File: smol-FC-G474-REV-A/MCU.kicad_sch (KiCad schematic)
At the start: 1 part, among them U1 STM32G474RETx

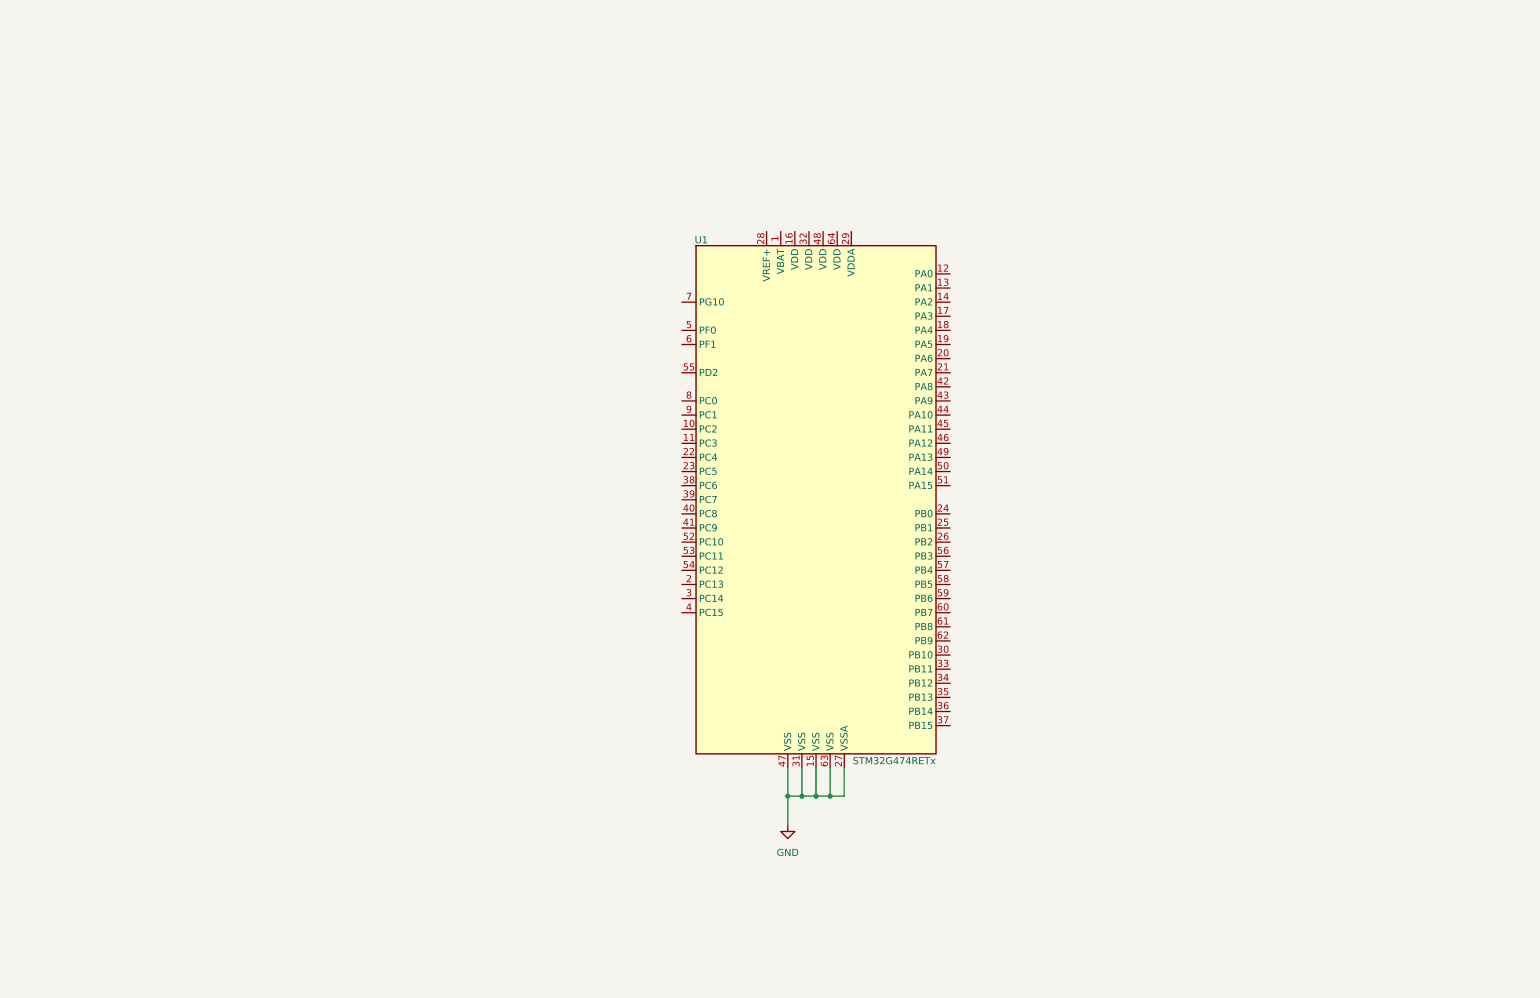
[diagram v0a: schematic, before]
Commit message: added USB-C section
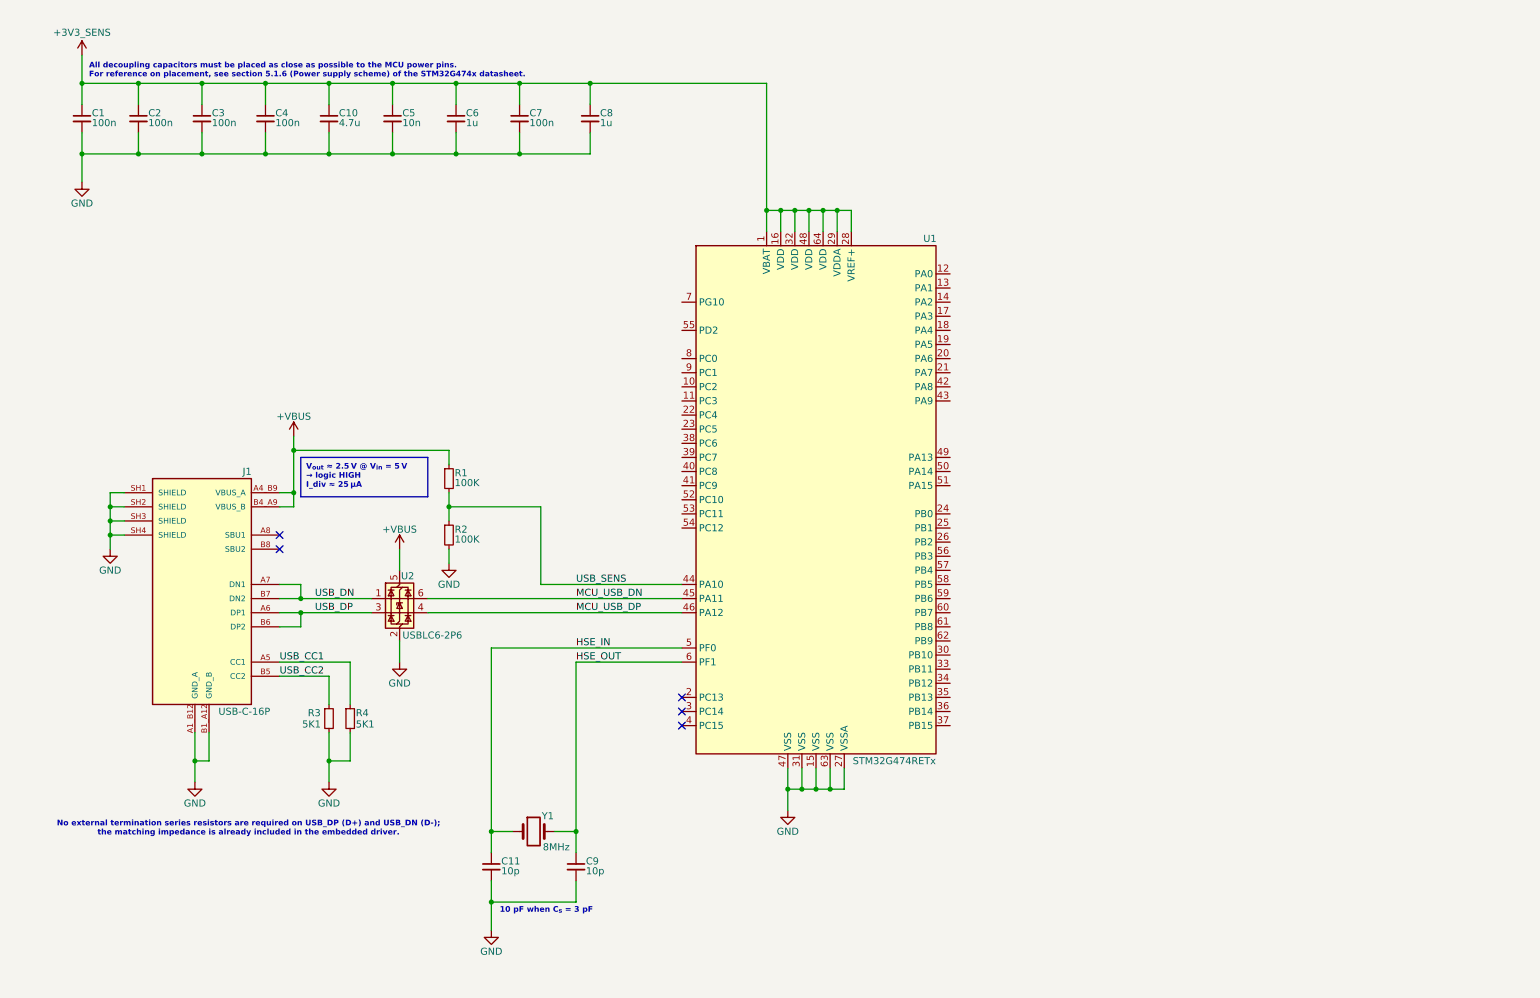
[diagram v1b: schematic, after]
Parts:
- added C1, C2, C3, C4, C7: 100n, symbol Device:C_Small
- added C10: 4.7u, symbol Device:C_Small
- added C11, C9: 10p, symbol Device:C_Small
- added C5: 10n, symbol Device:C_Small
- added C6, C8: 1u, symbol Device:C_Small
- added J1: USB-C-16P, TYPE-C_16PIN_2MD__073_:SHOUHAN_TYPE-C_16PIN_2MD__073_, symbol TYPE-C_16PIN_2MD__073_:TYPE-C_16PIN_2MD__073_
- added R1, R2: 100K, symbol Device:R_Small
- added R3, R4: 5K1, symbol Device:R_Small
- added U2: USBLC6-2P6, Package_TO_SOT_SMD:SOT-666, symbol Power_Protection:USBLC6-2P6
- added Y1: 8MHz, symbol Device:Crystal
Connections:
- net GND: now also C1.2, C10.2, C11.2, C2.2, C3.2, C4.2, C5.2, C6.2, C7.2, C8.2, C9.2, J1.A1_B12 (GND_A), J1.B1_A12 (GND_B), J1.SH1 (SHIELD), J1.SH2 (SHIELD), J1.SH3 (SHIELD), J1.SH4 (SHIELD), R2.2, R3.2, R4.2, U2.2 (GND)
- net +3V3_SENS: now reaches U1.1 (VBAT)
- net +3V3_SENS: now also U1.16 (VDD), U1.28 (VREF+), U1.29 (VDDA), U1.32 (VDD), U1.48 (VDD), U1.64 (VDD), C1.1, C10.1, C2.1, C3.1, C4.1, C5.1, C6.1, C7.1, C8.1
- net USB_SENS: now reaches U1.44 (PA10)
- net USB_SENS: now also R1.2, R2.1
- net MCU_USB_DN: now reaches U1.45 (PA11)
- net MCU_USB_DN: now also U2.6 (I/O1)
- net MCU_USB_DP: now reaches U1.46 (PA12)
- net MCU_USB_DP: now also U2.4 (I/O2)
- net HSE_IN: now reaches U1.5 (PF0)
- net HSE_IN: now also C11.1, Y1.1
- net HSE_OUT: now reaches U1.6 (PF1)
- net HSE_OUT: now also C9.1, Y1.2
- new net +VBUS: J1.A4_B9 (VBUS_A), J1.B4_A9 (VBUS_B), R1.1, U2.5 (VBUS)
- new net USB_CC1: J1.A5 (CC1), R4.1
- new net USB_CC2: J1.B5 (CC2), R3.1
- new net USB_DN: J1.A7 (DN1), J1.B7 (DN2), U2.1 (I/O1)
- new net USB_DP: J1.A6 (DP1), J1.B6 (DP2), U2.3 (I/O2)
- no-connect marks 0 -> 5
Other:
- note added: "10 pF when C_{s} = 3 pF"
- note added: "All decoupling capacitors must be placed as close as possible to the MCU power pins. For reference on placement, see section 5.1.6 (Power supply scheme) of the STM32G474x datasheet."
- note added: "No external termination series resistors are required on USB_DP (D+) and USB_DN (D-); the matching impedance is already included in the embedded driver."

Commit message: Schematic update
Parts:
- added 3V3_CORE, GND, NRST, SWCLK, SWDIO: TestPoint, symbol Connector:TestPoint
- added C10, C11, C14: 100n, symbol Device:C_Small
- added D1, D2, D3: LED, symbol Device:LED
- added D4: ESD, ESDALC6V1-1U2:DIODE_ESDALC6V1-1U2, symbol ESDALC6V1-1U2:ESDALC6V1-1U2
- added D5: RED, symbol Device:LED
- added R1, R12, R2, R3: 1K, symbol Device:R_Small
- added R10, R11, R5: 10K, symbol Device:R_Small
- added R4: 100K, symbol Device:R_Small
- added SW1: BOOT, symbol Switch:SW_Push
- renumbered C11 to C12, C9 to C13, C10 to C5, C5 to C6, C6 to C7, C7 to C8, C8 to C9, R1 to R6, R2 to R7, R3 to R8, R4 to R9
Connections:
- net GND: now also C10.2, C11.2, C14.2, D4.2, D5.1 (K), GND.1, R10.2, R5.2
- net M3: now reaches U1.10 (PC2)
- net M4: now reaches U1.11 (PC3)
- net ADC_CURR: now reaches U1.12 (PA0)
- net ADC_CURR: now also C11.1
- net ADC_VBAT: now reaches U1.13 (PA1)
- net ADC_VBAT: now also C10.1, R4.2, R5.1
- net TX2 (VTX): now reaches U1.14 (PA2)
- net RX2 (VTX): now reaches U1.17 (PA3)
- net SPI1_CS (OSD): now reaches U1.18 (PA4)
- net SPI1_SCK (OSD): now reaches U1.19 (PA5)
- net SPI1_MISO (OSD): now reaches U1.20 (PA6)
- net SPI1_MOSI (OSD): now reaches U1.21 (PA7)
- net LED_A: now reaches U1.22 (PC4)
- net LED_A: now also D3.1 (K)
- net LED_G: now reaches U1.23 (PC5)
- net LED_G: now also D2.1 (K)
- net LED_B: now reaches U1.24 (PB0)
- net LED_B: now also D1.1 (K)
- net LED: now reaches U1.25 (PB1)
- net AUX: now reaches U1.26 (PB2)
- net TX3 (ELRS): now reaches U1.30 (PB10)
- net RX3 (ELRS): now reaches U1.33 (PB11)
- net SPI2_CS (IMU): now reaches U1.34 (PB12)
- net SPI2_SCK (IMU): now reaches U1.35 (PB13)
- net SPI2_MISO (IMU): now reaches U1.36 (PB14)
- net SPI2_MOSI (IMU): now reaches U1.37 (PB15)
- net I2C4_SCL (BARO): now reaches U1.38 (PC6)
- net I2C4_SDA (BARO): now reaches U1.39 (PC7)
- net IMU_IRQ: now reaches U1.40 (PC8)
- net I2C3_SDA: now reaches U1.41 (PC9)
- net I2C3_SCL: now reaches U1.42 (PA8)
- net Buzzer: now reaches U1.43 (PA9)
- net SWDIO: now reaches U1.49 (PA13)
- net SWDIO: now also SWDIO.1
- net SWCLK: now reaches U1.50 (PA14)
- net SWCLK: now also SWCLK.1
- net SPI3_CS (Blackbox): now reaches U1.51 (PA15)
- net TX4 (GPS): now reaches U1.52 (PC10)
- net RX4 (GPS): now reaches U1.53 (PC11)
- net TX5 (TEL): now reaches U1.54 (PC12)
- net RX5 (TEL): now reaches U1.55 (PD2)
- net SPI3_SCK (Blackbox): now reaches U1.56 (PB3)
- net SPI3_MISO (Blackbox): now reaches U1.57 (PB4)
- net SPI3_MOSI (Blackbox): now reaches U1.58 (PB5)
- net TX1: now reaches U1.59 (PB6)
- net RX1: now reaches U1.60 (PB7)
- net BOOT: now reaches U1.61 (PB8)
- net BOOT: now also D4.1, R10.1, SW1.1
- net CC: now reaches U1.62 (PB9)
- net NRST: now reaches U1.7 (PG10)
- net NRST: now also C14.1, NRST.1, R11.2
- net M1: now reaches U1.8 (PC0)
- net M2: now reaches U1.9 (PC1)
- net +3V3_SENS renamed +3V3_CORE
- net +3V3_CORE: now also 3V3_CORE.1, R1.1, R11.1, R12.1, R2.1, R3.1, SW1.2
- new net +VBAT: R4.1
- new net LED_A_R: D3.2 (A), R3.2
- new net LED_B_R: D1.2 (A), R1.2
- new net LED_G_R: D2.2 (A), R2.2
- new net LED_PWR: D5.2 (A), R12.2
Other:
- note added: "ADC"
- note added: "BOOT Button"
- note added: "Blue, Green, Amber"
- note added: "C10 and C11 close to relevant MCU pin"
- note added: "C36 close to relevant MCU pin"
- note added: "D4 - ESDALC6V1-1U2"
- note added: "Debug"
- note added: "Decoupling Capacitors"
- note added: "HSE"
- note added: "Power LED"
- note added: "STATUS_LED"
- note added: "USB"
- moved on the sheet: C1, C12, C13, C2, C3, C4, C5, C6, C7, C8, C9, J1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

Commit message: complete connectors layout and initialize buck converter section. Added buck docs in /docs.
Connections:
- net TX5 (TEL): no longer names the net of U1.54 (PC12)
- no-connect marks 5 -> 6
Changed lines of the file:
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@@
 	(title_block
 		(title "smol-FC-G474")
-		(date "2026-05-24")
-		(rev "0.0.1")
+		(date "2026-05-31")
+		(rev "0.7.0")
 		(company "Daniel Plewa")
 		(comment 1 "License: CERN-OHL-W v2")
@@
 		(at 127 151.13)
 	)
+	(no_connect
+		(at 175.26 113.03)
+	)
 	(wire
 		(pts
@@
 		(effects
 			(font
-				(size 1.27 1.27)
-			)
-			(justify left)
-		)
-	)
-	(hierarchical_label "TX5 (TEL)"
-		(shape output)
-		(at 175.26 113.03 0)
-		(effects
-			(font

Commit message: Updated Buck-5V doc, added Buck 5V/10V and LDO for 3v3 on schematic
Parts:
- renumbered 3V3_CORE to 3V3_CORE1, GND to GND2, NRST to NRST1, SWCLK to SWCLK1, SWDIO to SWDIO1
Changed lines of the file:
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@@
 	(text "D4 - ESDALC6V1-1U2"
 		(exclude_from_sim no)
-		(at 252.476 119.126 0)
+		(at 246.634 119.126 0)
 		(effects
 			(font
@@
 		(in_pos_files yes)
 		(dnp no)
-		(property "Reference" "GND"
+		(property "Reference" "GND2"
 			(at 266.446 59.436 0)
 			(show_name no)
@@
 			(project "smol-FC-G474-REV-A"
 				(path "/650874a8-efa2-4da6-bfd2-a5dde0a9b2ac/1fef05e5-4b48-4307-88a4-eb5e10ad1d18"
-					(reference "GND")
+					(reference "GND2")
 					(unit 1)
 				)
@@
 		(in_pos_files yes)
 		(dnp no)
-		(property "Reference" "SWCLK"
+		(property "Reference" "SWCLK1"
 			(at 261.366 51.816 0)
 			(show_name no)
@@
 			(project "smol-FC-G474-REV-A"
 				(path "/650874a8-efa2-4da6-bfd2-a5dde0a9b2ac/1fef05e5-4b48-4307-88a4-eb5e10ad1d18"
-					(reference "SWCLK")
+					(reference "SWCLK1")
 					(unit 1)
 				)
@@
 		(in_pos_files yes)
 		(dnp no)
-		(property "Reference" "3V3_CORE"
+		(property "Reference" "3V3_CORE1"
 			(at 256.286 44.196 0)
 			(show_name no)
@@
 			(project "smol-FC-G474-REV-A"
 				(path "/650874a8-efa2-4da6-bfd2-a5dde0a9b2ac/1fef05e5-4b48-4307-88a4-eb5e10ad1d18"
-					(reference "3V3_CORE")
+					(reference "3V3_CORE1")
 					(unit 1)
 				)
@@
 		(in_pos_files yes)
 		(dnp no)
-		(property "Reference" "NRST"
+		(property "Reference" "NRST1"
 			(at 263.906 55.626 0)
 			(show_name no)
@@
 			(project "smol-FC-G474-REV-A"
 				(path "/650874a8-efa2-4da6-bfd2-a5dde0a9b2ac/1fef05e5-4b48-4307-88a4-eb5e10ad1d18"
-					(reference "NRST")
+					(reference "NRST1")
 					(unit 1)
 				)
@@
 		(in_pos_files yes)
 		(dnp no)
-		(property "Reference" "SWDIO"
+		(property "Reference" "SWDIO1"
 			(at 258.826 48.006 0)
 			(show_name no)
@@
 			(project "smol-FC-G474-REV-A"
 				(path "/650874a8-efa2-4da6-bfd2-a5dde0a9b2ac/1fef05e5-4b48-4307-88a4-eb5e10ad1d18"
-					(reference "SWDIO")
+					(reference "SWDIO1")
 					(unit 1)
 				)

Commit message: Changed 10V buck to 9V buck
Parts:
- D4: footprint ESDALC6V1-1U2:DIODE_ESDALC6V1-1U2 -> (none)
- J1: footprint TYPE-C_16PIN_2MD__073_:SHOUHAN_TYPE-C_16PIN_2MD__073_ -> (none)
- U1: footprint Package_QFP:LQFP-64_10x10mm_P0.5mm -> (none)
- U2: footprint Package_TO_SOT_SMD:SOT-666 -> (none)
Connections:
- net MCU_USB_DN renamed MCU_USB_D_N
- net MCU_USB_DP renamed MCU_USB_D_P
- net USB_DN renamed USB_D_N
- net USB_DP renamed USB_D_P
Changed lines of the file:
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@@
 		)
 	)
-	(label "USB_DP"
+	(label "USB_D_P"
 		(at 60.96 134.62 0)
 		(effects
@@
 		)
 	)
-	(label "MCU_USB_DP"
+	(label "MCU_USB_D_P"
 		(at 107.95 134.62 0)
 		(effects
@@
 		)
 	)
-	(label "MCU_USB_DN"
+	(label "MCU_USB_D_N"
 		(at 107.95 132.08 0)
 		(effects
@@
 		)
 	)
-	(label "USB_DN"
+	(label "USB_D_N"
 		(at 60.96 132.08 0)
 		(effects
@@
 			)
 		)
-		(property "Footprint" "ESDALC6V1-1U2:DIODE_ESDALC6V1-1U2"
+		(property "Footprint" ""
 			(at 245.11 100.33 0)
 			(hide yes)
@@
 			)
 		)
-		(property "Footprint" "Package_TO_SOT_SMD:SOT-666"
+		(property "Footprint" ""
 			(at 77.216 138.811 0)
 			(hide yes)
@@
 			)
 		)
-		(property "Footprint" "TYPE-C_16PIN_2MD__073_:SHOUHAN_TYPE-C_16PIN_2MD__073_"
+		(property "Footprint" ""
 			(at 42.926 96.52 0)
 			(hide yes)
@@
 			)
 		)
-		(property "Footprint" "Package_QFP:LQFP-64_10x10mm_P0.5mm"
+		(property "Footprint" ""
 			(at 135.89 158.75 0)
 			(hide yes)
